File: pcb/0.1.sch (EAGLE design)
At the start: 64 parts, among them Q3 BSS123, Q4 BSS123, U1 PIC18LF13K22-I/SS, U2 IR2183, U3 V_REG_317SMD, U4 INA-139, U5 INA-139, U6 INA-139, X1 TXC-7A

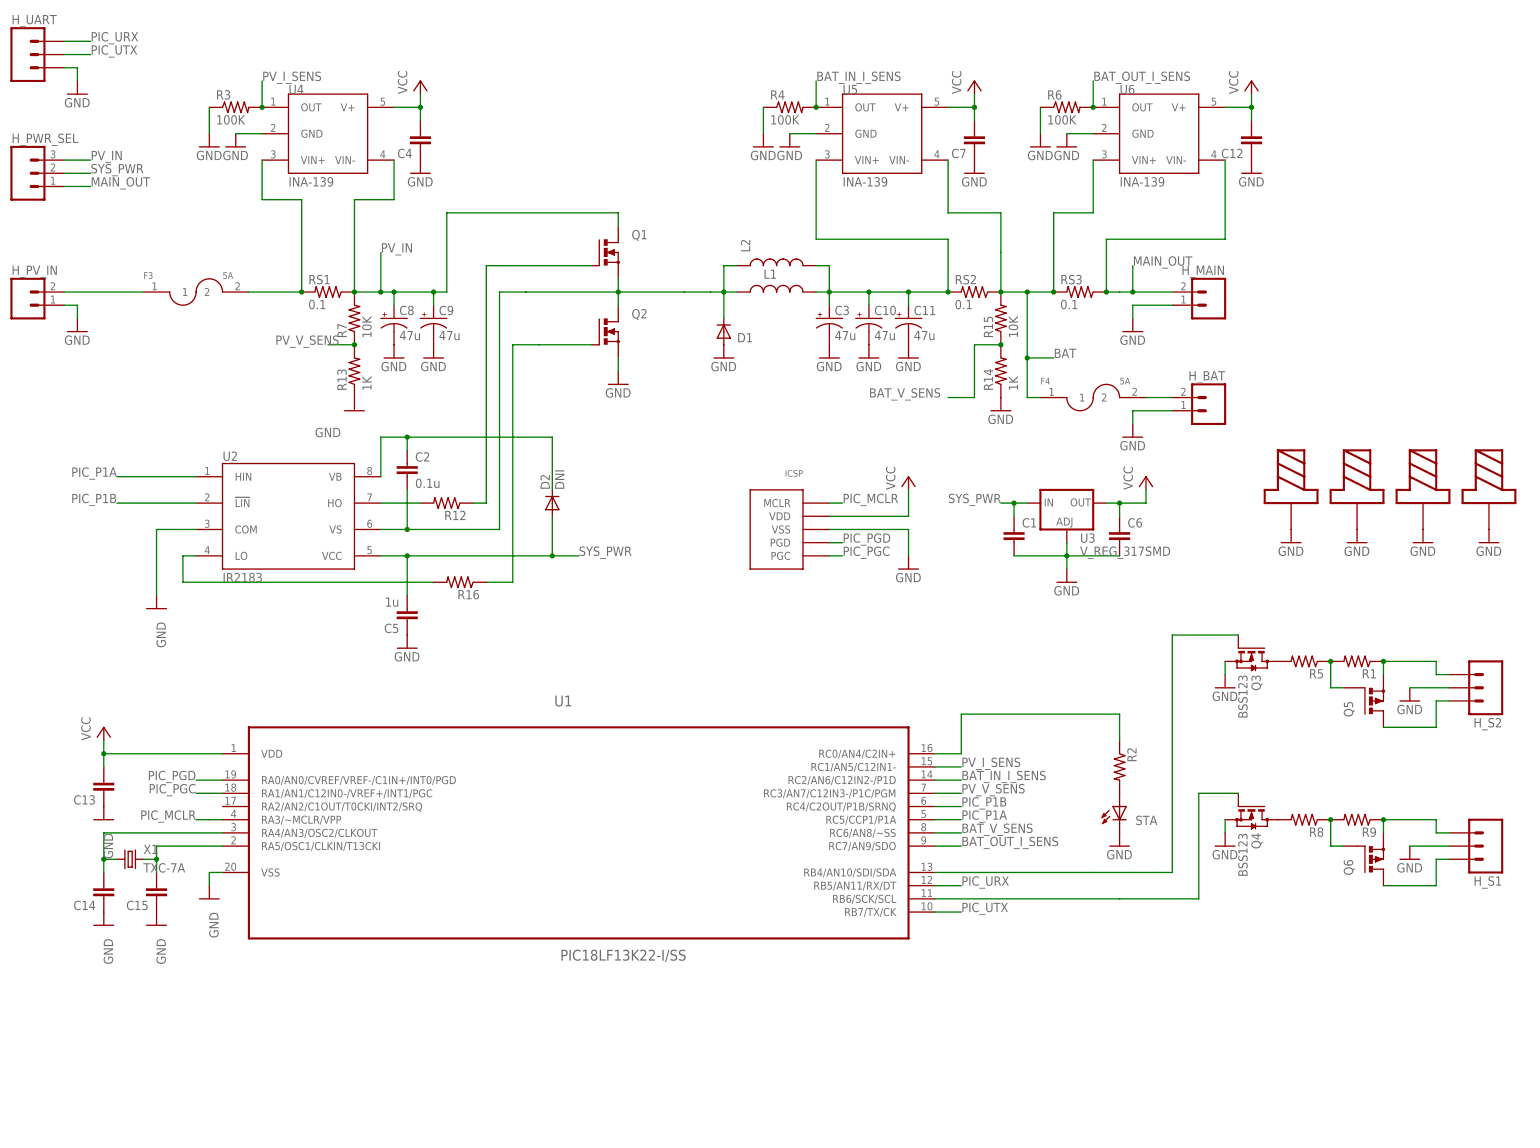
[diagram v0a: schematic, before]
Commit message: Removed some functions no longer used, added a few code comments, changed the file structure.
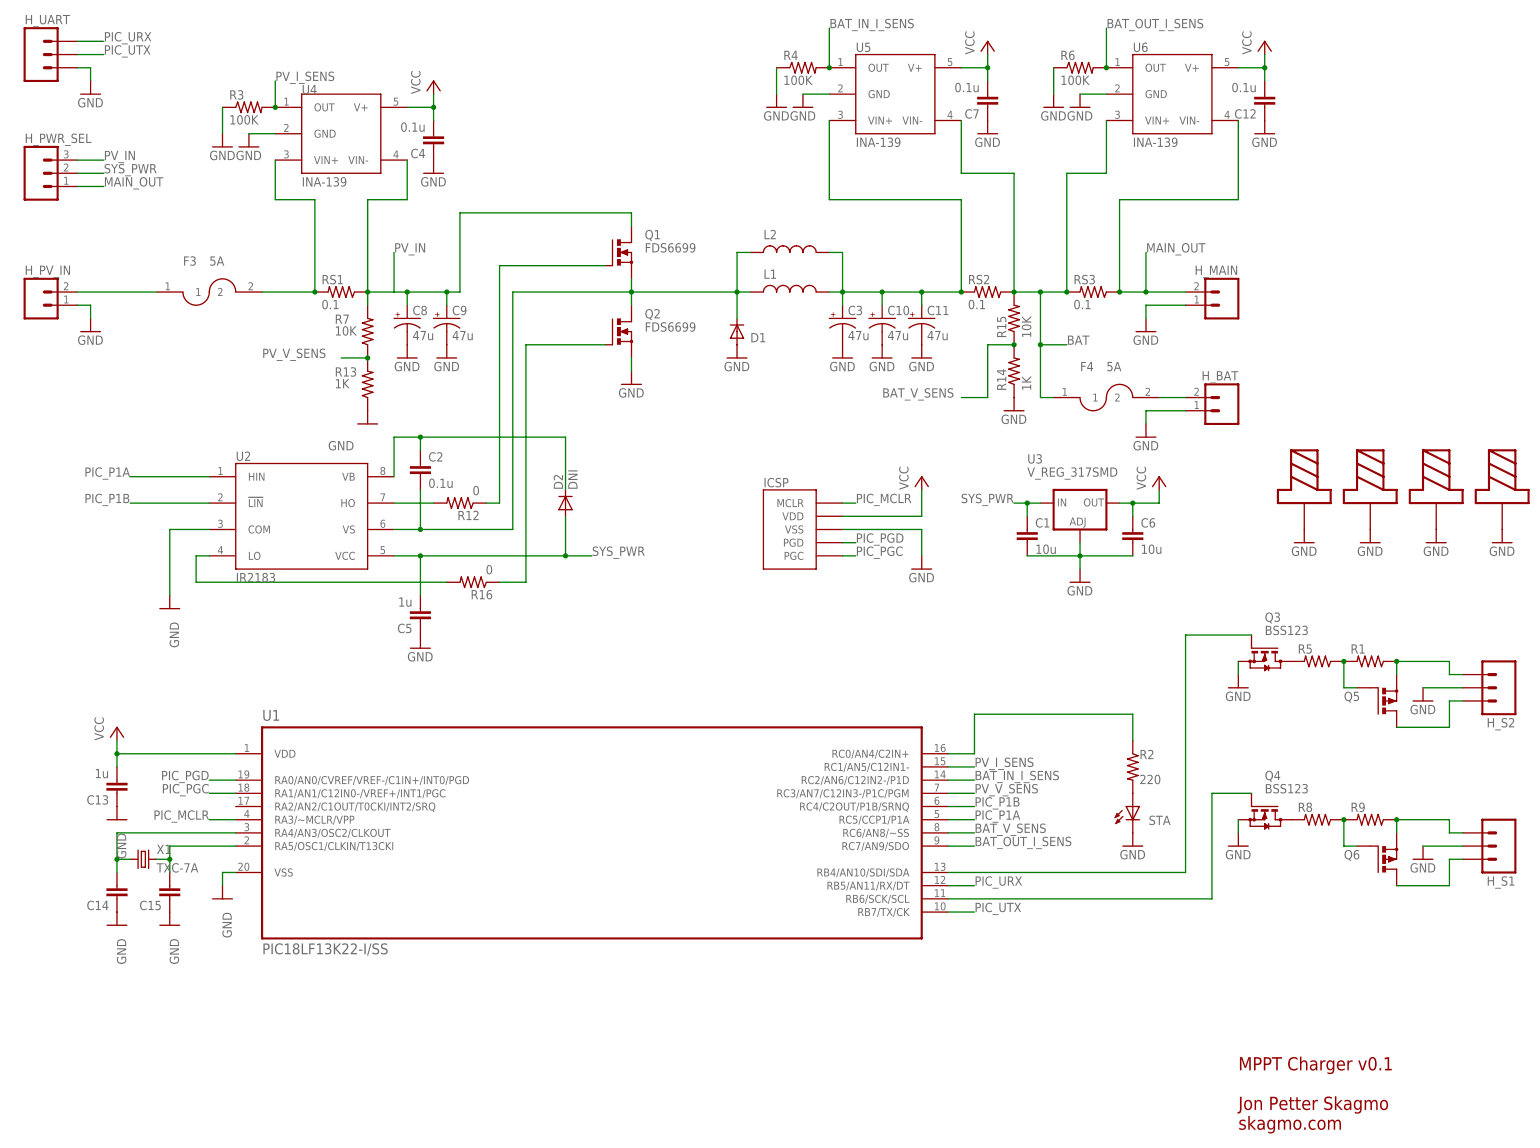
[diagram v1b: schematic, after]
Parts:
- C1, C6: value (none) -> 10u
- C12, C4, C7: value (none) -> 0.1u
- C13: value (none) -> 1u
- Q1, Q2: value (none) -> FDS6699
- R12, R16: value (none) -> 0
- R2: value (none) -> 220
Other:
- note added: "MPPT Charger v0.1 Jon Petter Skagmo skagmo.com"
- moved on the sheet: C1, C10, C11, C12, C13, C14, C15, C2, C3, C4, C5, C6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
